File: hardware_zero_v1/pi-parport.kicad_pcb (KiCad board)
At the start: 2 copper layers, 65 x 56 mm, 17 parts, among them J1 CONN_01X02, J2 40HAT, J3 Conn_02x13_Odd_Even, U1 CAT24C32, U2 SN74LVC161284DLR

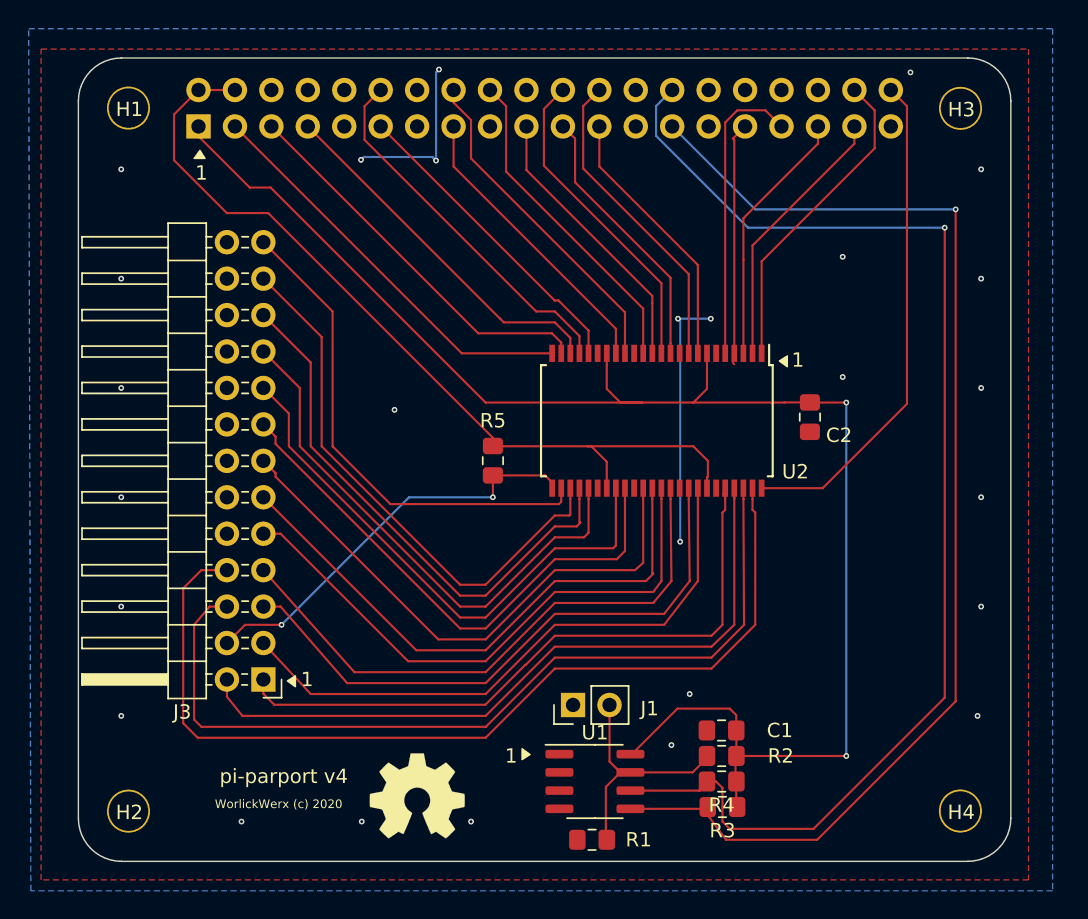
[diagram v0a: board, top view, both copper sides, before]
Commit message: First run at RPi Zero form factor.
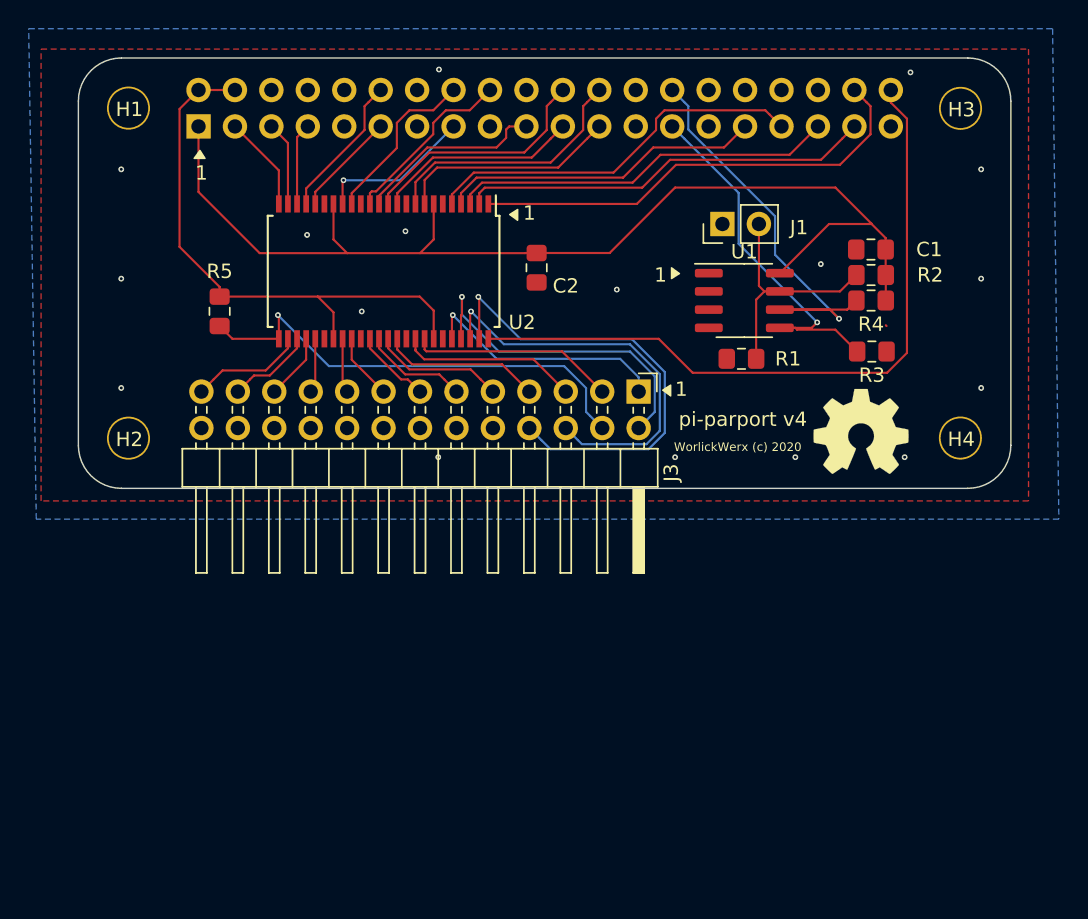
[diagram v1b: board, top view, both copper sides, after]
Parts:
- moved REF** 40.0 mm to (133.1, 86.9)
- moved J1 35.1 mm to (123.4, 72.4)
- moved R1 35.1 mm to (124.8, 81.8)
- moved R2 35.1 mm to (133.8, 75.9)
- moved C1 35.1 mm to (133.8, 74.2)
- moved R4 35.1 mm to (133.8, 77.7)
- moved U1 35.1 mm to (125.0, 77.7)
- moved R3 33.4 mm to (133.9, 81.3)
- moved J3 33.0 mm to (117.6, 84.1), turned to 270 degrees
- moved H2 26.0 mm to (82.0, 87.3)
- moved H4 26.0 mm to (140.0, 87.3)
- moved C2 21.7 mm to (110.5, 75.4)
- moved R5 21.7 mm to (88.4, 78.5)
- moved U2 21.7 mm to (99.8, 75.7)
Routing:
- net /ID_SD_EEPROM: track 85.7 -> 26.9 mm
- net /ID_SC_EEPROM: track 87.8 -> 30.8 mm
- net /DATA7: track 38.6 -> 3.81 mm
- net /STATUS6: track 37.7 -> 3.81 mm
- net /DATA5: track 39.2 -> 5.40 mm
- net /DATA6: track 38.2 -> 4.60 mm
- net /STATUS7: track 38.2 -> 4.60 mm
- net /CONTROL3: track 66.1 -> 32.9 mm, vias 0 -> 1
- net +3V3: track 110.2 -> 77.5 mm, vias 2 -> 0
- net /STATUS5: track 38.6 -> 6.04 mm
- net /DATA4: track 39.8 -> 7.31 mm
- net /CONTROL2: track 60.5 -> 28.3 mm, vias 0 -> 1
- net /DATA3: track 40.3 -> 9.21 mm
- net GND: track 29.7 -> 0.00 mm, vias 27 -> 17
- net /DATA2: track 40.8 -> 11.2 mm
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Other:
- board size 65 x 56 mm -> 65 x 30 mm
